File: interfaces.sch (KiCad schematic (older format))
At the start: 19 parts, among them J4 UEXT, J6 Screw_Terminal_1x02, P2 USB_B, P3 USB_OTG, U8 TJA1042T/3

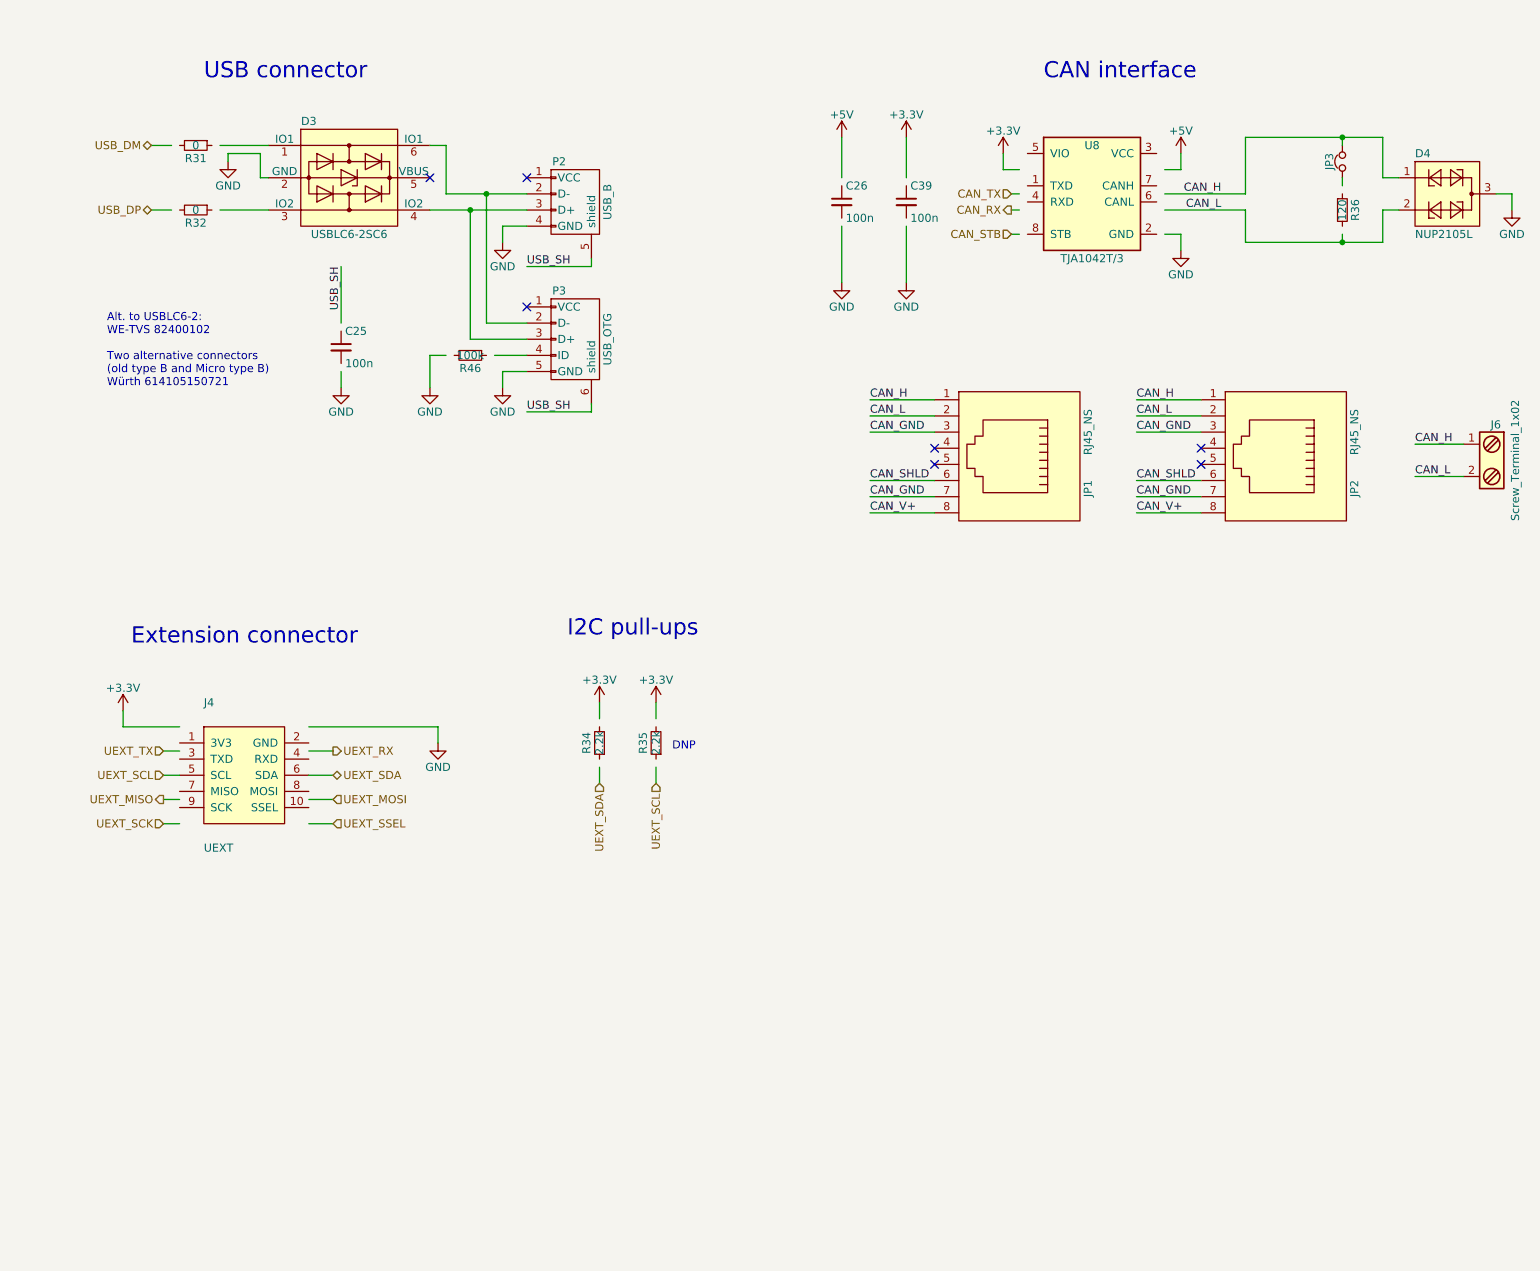
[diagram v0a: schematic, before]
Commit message: Updated R/C/L symbols to IEC 60617 style
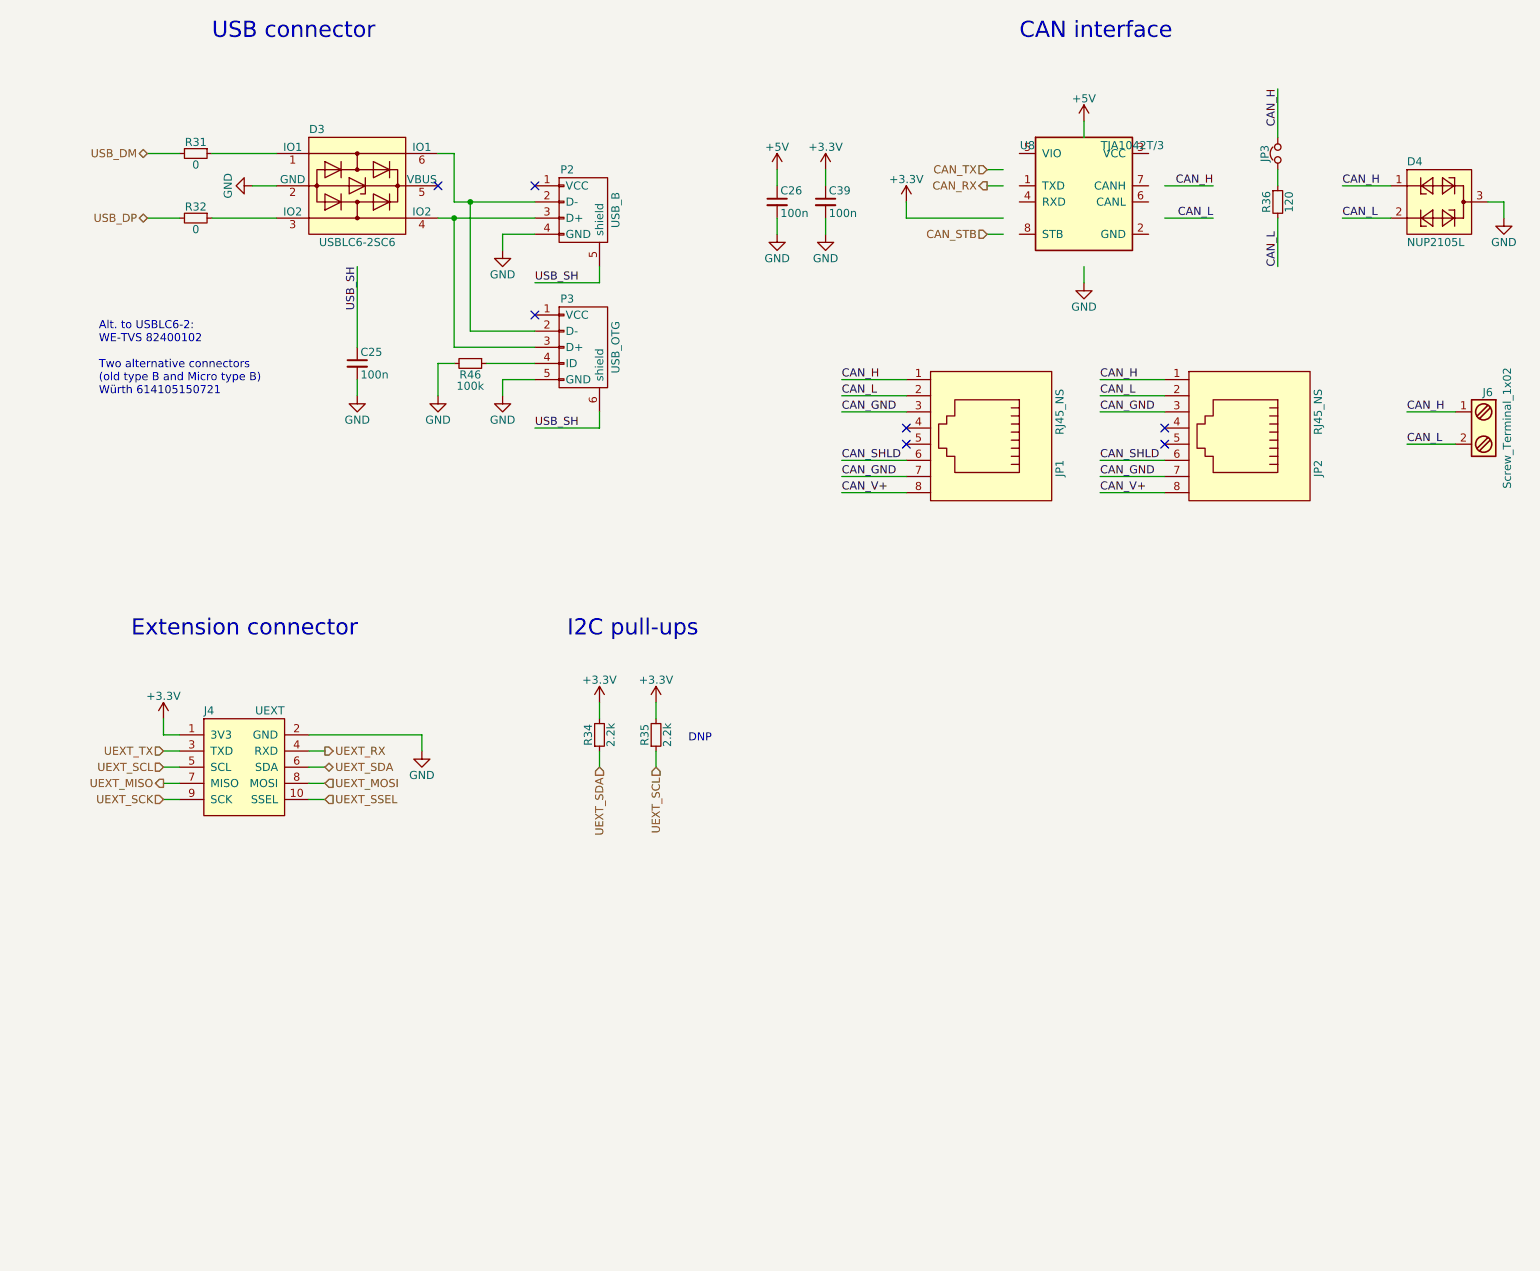
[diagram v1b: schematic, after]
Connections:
- wire segments 87 -> 76
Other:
- moved on the sheet: C25, C26, C39, D3, D4, J4, J6, JP1, JP2, JP3, P2, P3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

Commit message: Updated revision: 0.8
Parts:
- removed J6: Screw_Terminal_1x02, Connectors_Terminal_Blocks:TerminalBlock_Pheonix_MKDS1.5-2pol, symbol Screw_Terminal_1x02
- removed P2: USB_B, Connectors:USB_B, symbol USB_B-RESCUE-MPPT_charger_20A
- removed R31, R32: 0, Resistors_SMD:R_0603, symbol R
- added D10, D9: 1N4148, LibreSolar:D_SOD-123, symbol D
- added Q5: BSS84, LibreSolar:SOT-23, symbol Q_PMOS_GSD
- added R33, R47: 100k, LibreSolar:R_0603_1608, symbol R
- added R38: 1k, LibreSolar:R_0603_1608, symbol R
- added RT2, RT3: 200mA, LibreSolar:R_1206_3216, symbol R_PTC
- added T4: MMBT3904, LibreSolar:SOT-23, symbol MMBT3904
- C25: footprint Capacitors_SMD:C_0603 -> LibreSolar:C_0603_1608; MFR Murata -> (none); MPN GRM188R71H104KA93D -> (none); Manufacturer (none) -> Murata; PartNumber (none) -> GRM188R71H104KA93D; SPN - -> (none); SPR - -> (none); SPURL - -> (none)
- C26, C39: footprint Capacitors_SMD:C_0603 -> LibreSolar:C_0603_1608; MFR Murata -> (none); MPN GRM188R71H104KA93D -> (none); Manufacturer (none) -> Murata; PartNumber (none) -> GRM188R71H104KA93D
- D3: footprint TO_SOT_Packages_SMD:SOT-23-6 -> LibreSolar:SOT-23-6; MFR STMicroelectronics -> (none); MPN USBLC6-2SC6 -> (none); Manufacturer (none) -> STMicroelectronics; PartNumber (none) -> USBLC6-2SC6
- D4: footprint TO_SOT_Packages_SMD:SOT-23 -> LibreSolar:SOT-23; symbol NUP2105L-RESCUE-MPPT_charger_20A -> NUP2105L; MFR ON Semiconductor -> (none); MPN NUP2105LT1G -> (none); Manufacturer (none) -> ON Semiconductor; PartNumber (none) -> NUP2105LT1G
- J4: footprint Pin_Headers:Pin_Header_Straight_2x05_Pitch2.54mm -> LibreSolar:Box_Header_2x05x2.54mm_Straight
- JP1, JP2: footprint Connectors:RJ45_8 -> LibreSolar:RJ45_8P8C; MFR Amphenol FCI -> (none); MPN 54602-908LF -> (none); Manufacturer (none) -> Amphenol FCI; PartNumber (none) -> 54602-908LF
- P3: footprint LibreSolar:Wuerth_USB_Micro_USB_vert_Type_B_614105150721 -> LibreSolar:USB_Micro-B_10103594-0001LF; MFR Wuerth -> (none); MPN 614105150721 -> (none); Manufacturer (none) -> FCI; PartNumber (none) -> 10103594-0001LF
- R34, R35: footprint Resistors_SMD:R_0603 -> LibreSolar:R_0603_1608; MFR Yageo -> (none); MPN RC0603FR-072K2L -> (none); Manufacturer (none) -> Yageo; PartNumber (none) -> RC0603FR-072K2L
- R36: footprint Resistors_SMD:R_1206 -> LibreSolar:R_1206_3216; MFR Yageo -> (none); MPN RC1206FR-07120RL -> (none); Manufacturer (none) -> Yageo; PartNumber (none) -> RC1206FR-07120RL
- R46: footprint Resistors_SMD:R_0603 -> LibreSolar:R_0603_1608; MFR Yageo -> (none); MPN RC0603FR-07100KL -> (none); Manufacturer (none) -> Yageo; PartNumber (none) -> RC0603FR-07100KL
- U8: MFR NXP -> (none); MPN TJA1042T/3/1J -> (none); Manufacturer (none) -> NXP; PartNumber (none) -> TJA1042T/3/1J
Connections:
- net labels added: +10V, 5V_OUT, 5V_OUT_EN, RJ45_4, RJ45_5
- net labels removed: USB_SH
- wire segments 76 -> 95
- no-connect marks 7 -> 0
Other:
- note added: "5V signal output"
- note removed: "Alt. to USBLC6-2:\nWE-TVS 82400102\n\nTwo alternative connectors\n(old type B and Micro type B)\nWürth 614105150721"
- note removed: "DNP"
- moved on the sheet: C25, C26, C39, D3, J4, JP3, P3, R34, R35, R36, R46

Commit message: V0.8.1: Small changes and update to new kicad symbol library table (nightlies only)
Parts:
- C25, C26, C39: symbol C -> device:C_Small
- D10, D9: symbol D -> device:D_Small
- D3: symbol USBLC6-2SC6 -> LibreSolar:USBLC6-2SC6
- D4: symbol NUP2105L -> LibreSolar:NUP2105L
- F2: renamed from RT2; symbol R_PTC -> device:Polyfuse
- F3: renamed from RT3; symbol R_PTC -> device:Polyfuse
- J4: symbol UEXT -> LibreSolar:UEXT
- JP1, JP2: symbol RJ45_NS -> LibreSolar:RJ45_NS
- JP3: symbol Jumper_NC_Small -> device:Jumper_NC_Small
- P3: value USB_OTG -> USB Micro B; symbol USB_OTG-RESCUE-MPPT_charger_20A -> Connector:USB_B_Micro
- Q5: symbol Q_PMOS_GSD -> device:Q_PMOS_GSD
- R33, R34, R35, R36, R38, R46, R47: symbol R -> device:R_Small
- T4: symbol MMBT3904 -> Transistor:BC817
- U8: footprint Housings_SOIC:SOIC-8_3.9x4.9mm_Pitch1.27mm -> LibreSolar:SOIC-8_3.9x4.9mm_Pitch1.27mm; symbol TJA1042T/3 -> LibreSolar:TJA1042T-3
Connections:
- net GND: now also C25.2; no longer C25.1
- net at P3.6 (Shield): now also C25.1; no longer C25.2
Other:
- moved on the sheet: C25, JP2

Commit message: Bus power supply from battery instead of 10V rail
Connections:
- net +10V renamed DCDC_OUT
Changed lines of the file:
@@
-$EndComp
-$Comp
-L LibreSolar:+10V #PWR073
-U 1 1 5954FF10
-P 7300 4900
-F 0 "#PWR073" H 7300 4750 50  0001 C CNN
-F 1 "+10V" H 7300 5040 50  0000 C CNN
-F 2 "" H 7300 4900 50  0000 C CNN
-F 3 "" H 7300 4900 50  0000 C CNN
-	1    7300 4900
-	1    0    0    -1
 $EndComp
 $Comp
@@
 Wire Wire Line
 	2900 1800 3050 1800
+Text HLabel 7300 4900 1    50   Input ~ 0
+DCDC_OUT
 $EndSCHEMATC

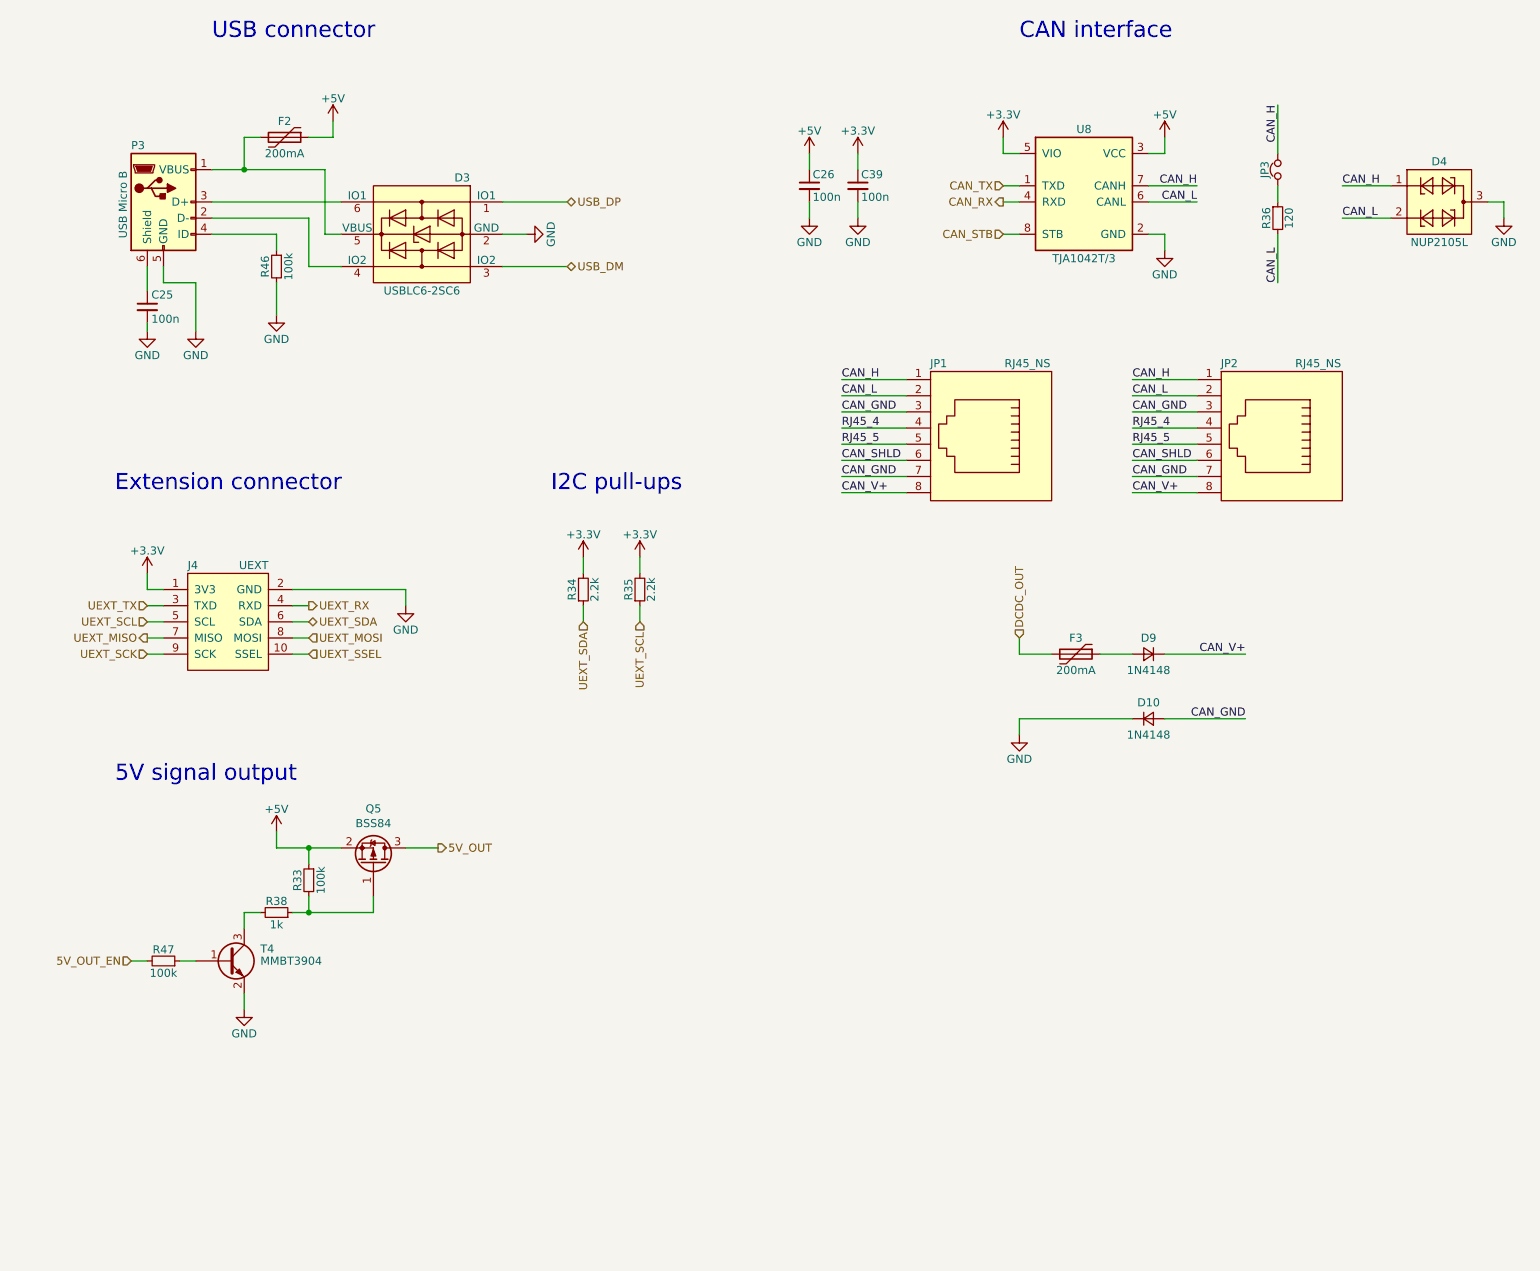
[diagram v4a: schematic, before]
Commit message: Revision 0.9 for first small production batch - Switchable power supply for bus and UEXT (to be make sure to reach very low power consumption during LVD conditions) - MLCCs for EMC added to each high power input/output - Re-arrangement of some connectors after initial tests with housing
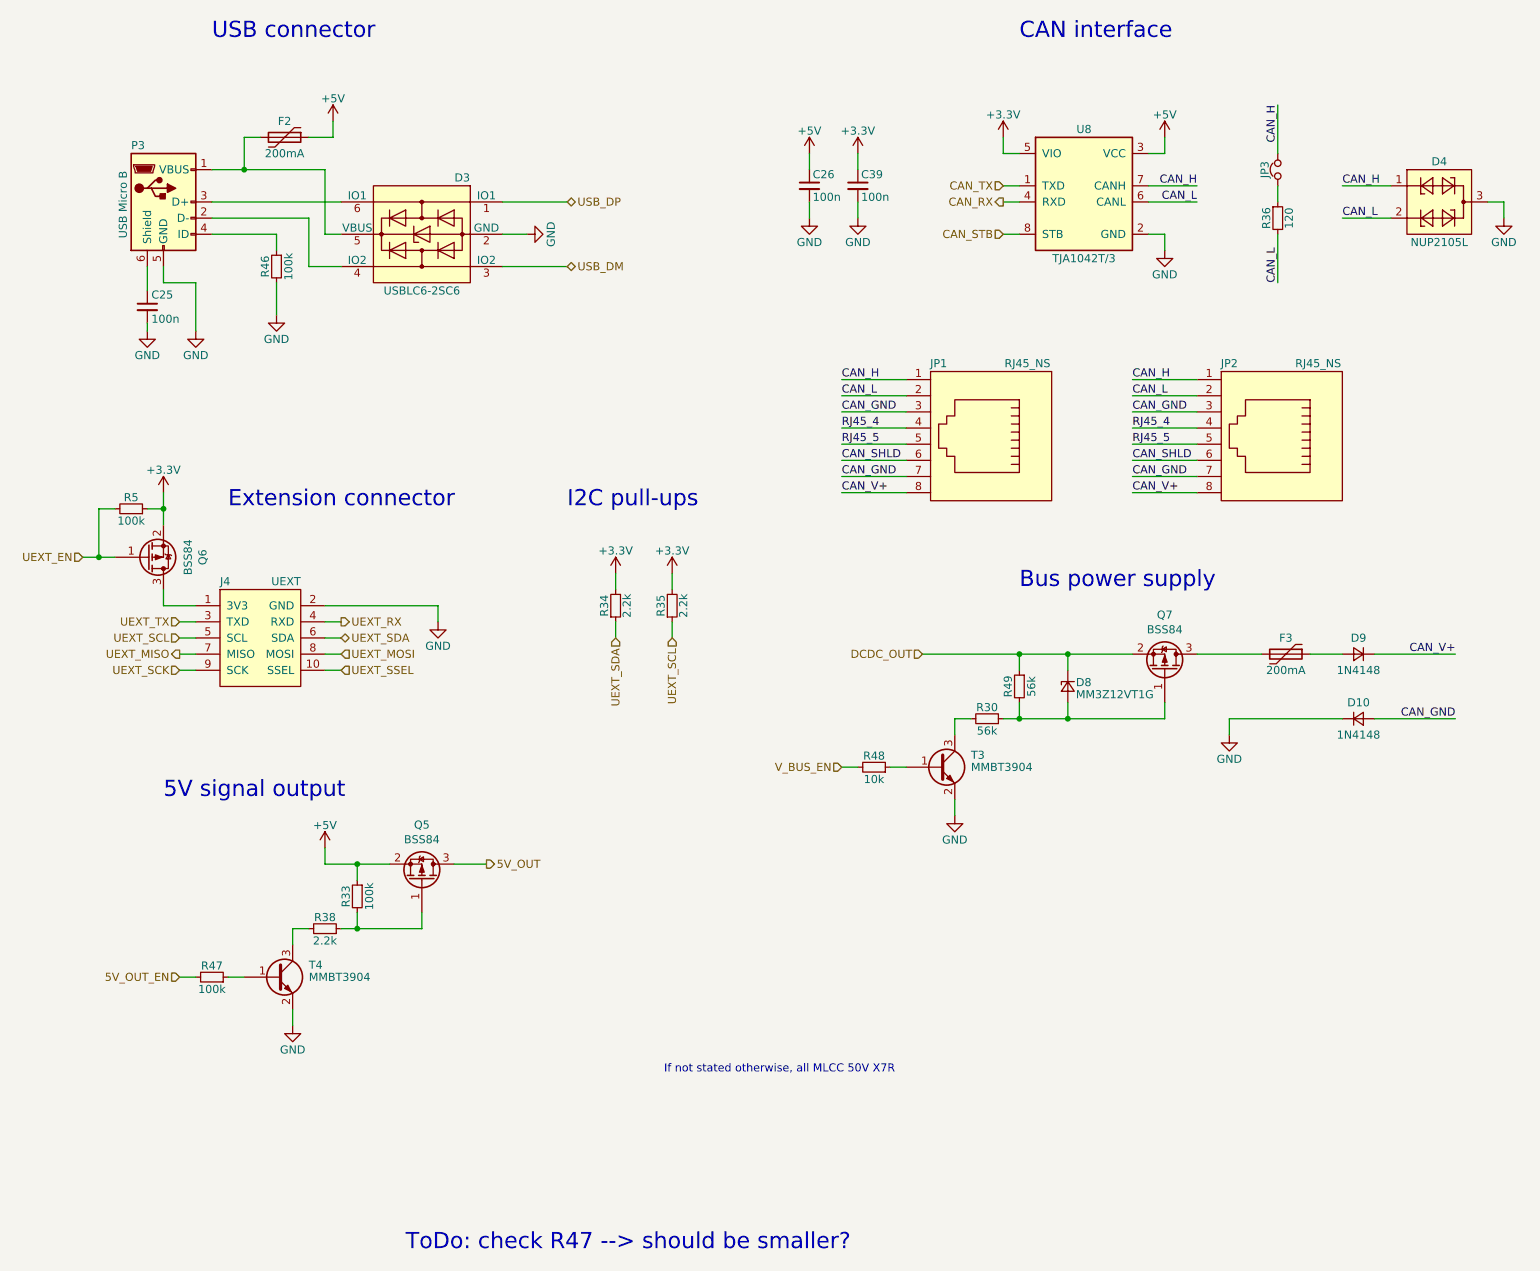
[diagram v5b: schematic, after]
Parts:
- added D8: MM3Z12VT1G, LibreSolar:D_SOD-323, symbol device:D_Zener_Small
- added Q6, Q7: BSS84, LibreSolar:SOT-23, symbol device:Q_PMOS_GSD
- added R30, R49: 56k, LibreSolar:R_0603_1608, symbol device:R_Small
- added R48: 10k, LibreSolar:R_0603_1608, symbol device:R_Small
- added R5: 100k, LibreSolar:R_0603_1608, symbol device:R_Small
- added T3: MMBT3904, LibreSolar:SOT-23, symbol Transistor:BC817
- JP3: footprint Pin_Headers:Pin_Header_Straight_1x02_Pitch2.54mm -> Pin_Headers:Pin_Header_Angled_1x02_Pitch2.54mm
- P3, U8: SPR Mouser -> (none); Supplier (none) -> Mouser
- R38: value 1k -> 2.2k; PartNumber RC0603FR-071KL -> RC0603FR-072K2L
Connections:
- net +3V3: now also Q6.2 (S), R5.1; no longer J4.1 (3V3)
- net CAN_H: now also JP3.1; no longer JP3.2
- net DCDC_OUT: now also D8.1 (K), Q7.2 (S), R49.1; no longer F3.2
- net GND: now also T3.2 (E)
- net at R36.1: now also JP3.2; no longer JP3.1
- new net: J4.1 (3V3), Q6.3 (D)
- new net: F3.2, Q7.3 (D)
- new net: D8.2 (A), Q7.1 (G), R30.1, R49.2
- new net: R30.2, T3.3 (C)
- new net: R48.1, T3.1 (B)
- new net UEXT_EN: Q6.1 (G), R5.2
- new net V_BUS_EN: R48.2
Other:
- note added: "Bus power supply"
- note added: "If not stated otherwise, all MLCC 50V X7R"
- note added: "ToDo: check R47 --> should be smaller?"
- moved on the sheet: D10, D9, F3, J4, Q5, R33, R34, R35, R38, R47, T4
